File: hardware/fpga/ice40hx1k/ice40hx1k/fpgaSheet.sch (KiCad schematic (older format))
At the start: 16 parts, among them U6 ICE40HX1K-VQ100(VQFP100)

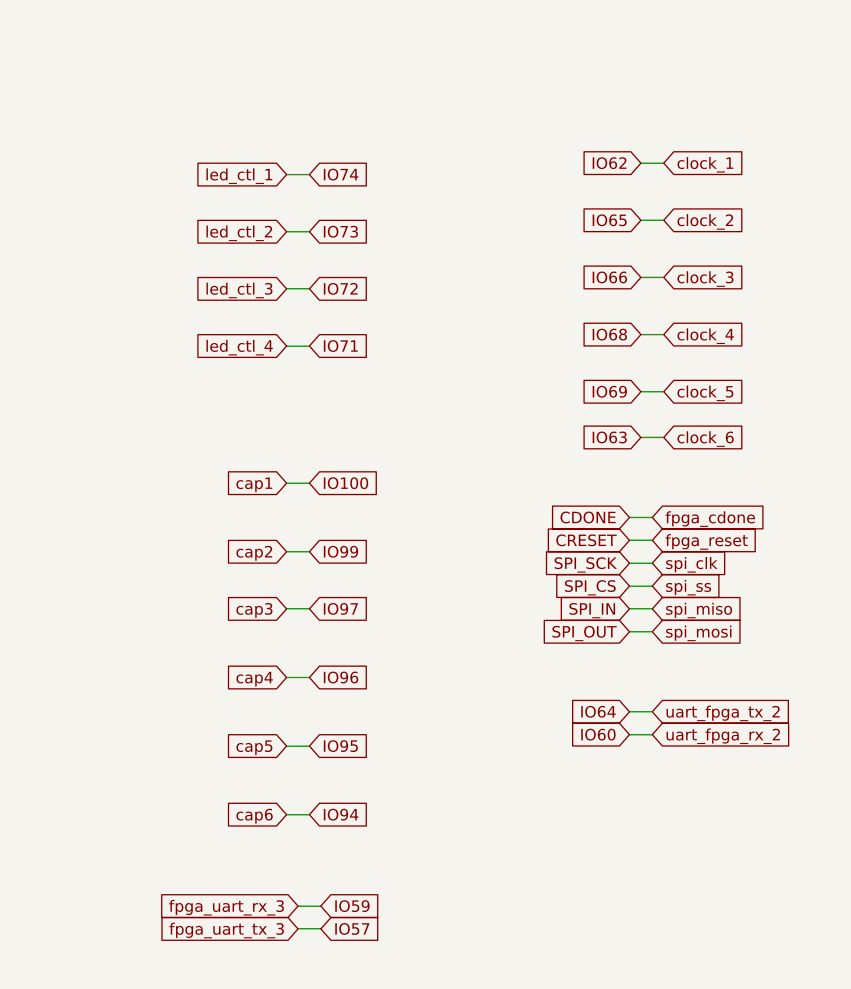
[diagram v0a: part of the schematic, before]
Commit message: std FPGA skeleton
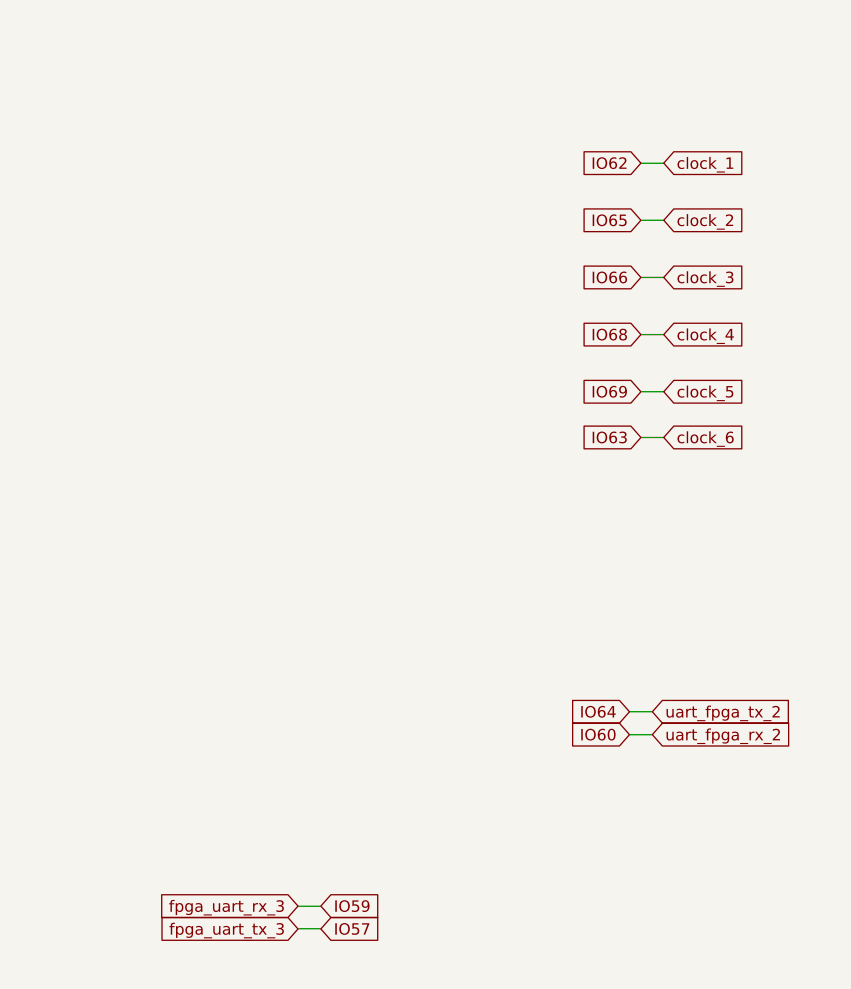
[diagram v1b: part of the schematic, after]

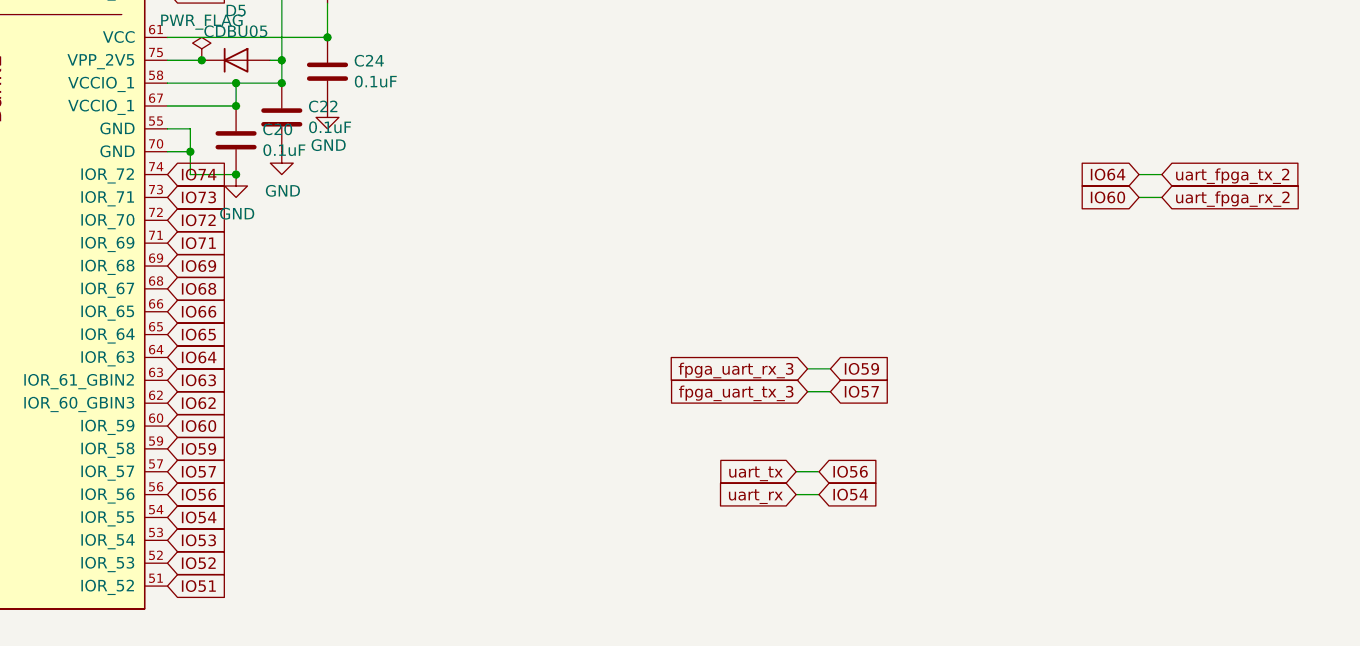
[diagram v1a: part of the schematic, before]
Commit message: std FPGA skeleton
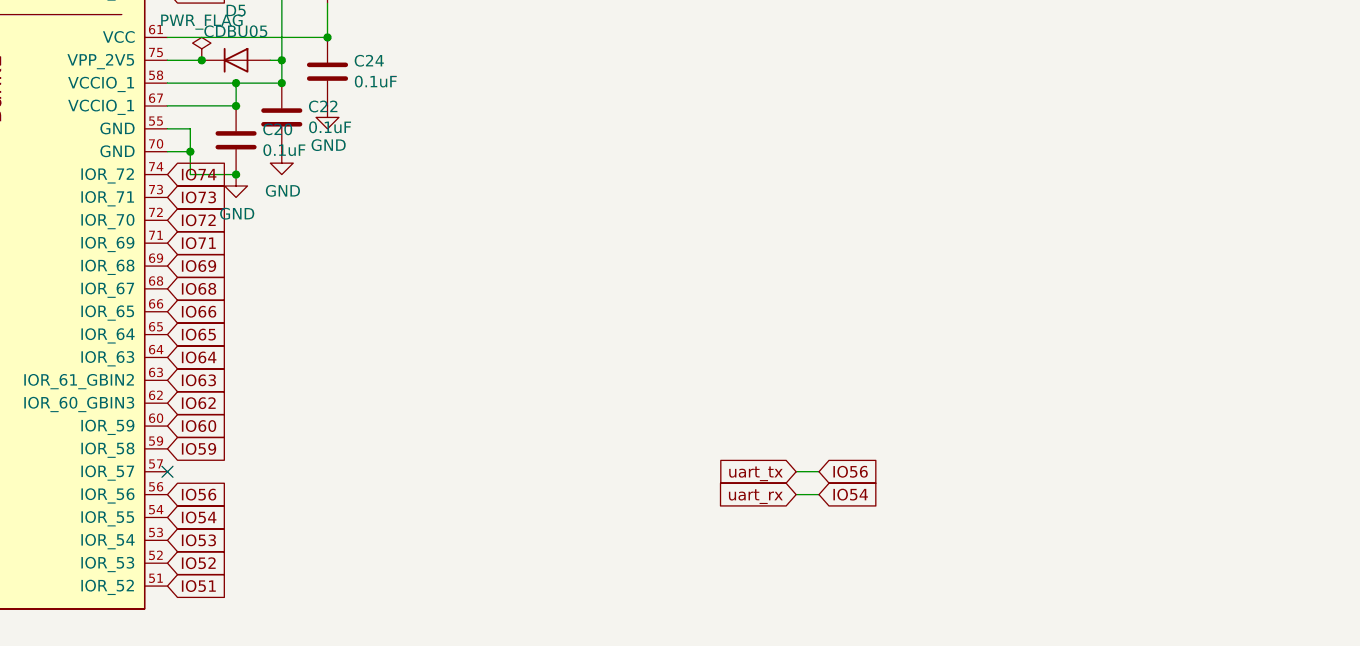
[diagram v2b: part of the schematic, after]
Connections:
- net IO57: no longer names the net of U6.57 (IOR_57)
- no-connect marks 1 -> 2
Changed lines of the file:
@@
 Text GLabel 4650 6000 2    50   Input ~ 0
 IO56
-Text GLabel 4650 5900 2    50   Input ~ 0
-IO57
 Text GLabel 4650 5800 2    50   Input ~ 0
 IO59
@@
 Text GLabel 9050 3400 2    50   Input ~ 0
 clock_6
-Text GLabel 7450 5450 0    50   Input ~ 0
-fpga_uart_rx_3
-Text GLabel 7450 5550 0    50   Input ~ 0
-fpga_uart_tx_3
-Text GLabel 9000 4600 2    50   Input ~ 0
-uart_fpga_tx_2
-Text GLabel 9000 4700 2    50   Input ~ 0
-uart_fpga_rx_2
 Text GLabel 7400 5900 0    50   Input ~ 0
 uart_tx
@@
 Text GLabel 7500 5900 2    50   Input ~ 0
 IO56
-Text GLabel 7550 5550 2    50   Input ~ 0
-IO57
-Text GLabel 7550 5450 2    50   Input ~ 0
-IO59
-Text GLabel 8900 4700 0    50   Input ~ 0
-IO60
-Text GLabel 8900 4600 0    50   Input ~ 0
-IO64
 Text GLabel 8950 2200 0    50   Input ~ 0
 IO62
@@
 Text GLabel 8950 3200 0    50   Input ~ 0
 IO69
-Wire Wire Line
-	7450 5450 7550 5450
-Wire Wire Line
-	7450 5550 7550 5550
 Wire Wire Line
 	7400 5900 7500 5900
@@
 Wire Wire Line
 	8950 3400 9050 3400
-Wire Wire Line
-	8900 4600 9000 4600
-Wire Wire Line
-	8900 4700 9000 4700
+NoConn ~ 4650 5900
 $EndSCHEMATC
